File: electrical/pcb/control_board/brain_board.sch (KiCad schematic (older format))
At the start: 7 parts, among them J10 6posheader, J27 PPTC102LFBN-RC, J6 S9175-ND_rpi_breakout, J7 S9175-ND_rpi_breakout, J8 6posheader

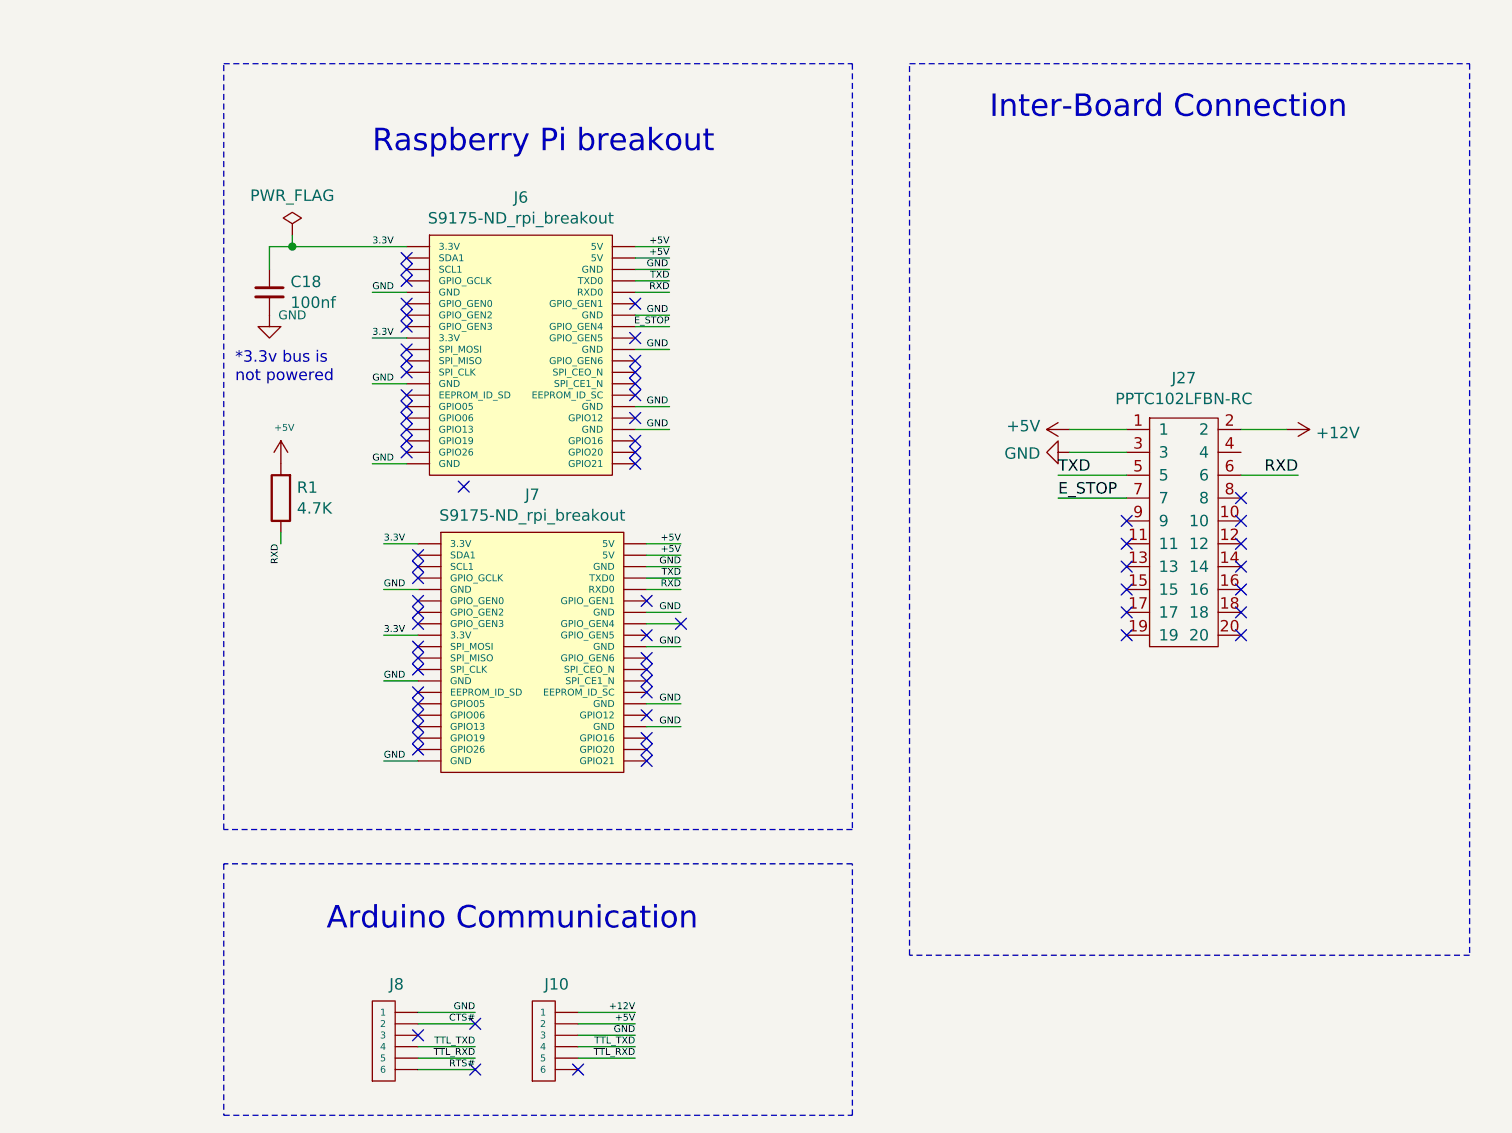
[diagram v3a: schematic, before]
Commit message: updating motor and brain boards with board-specific power nets
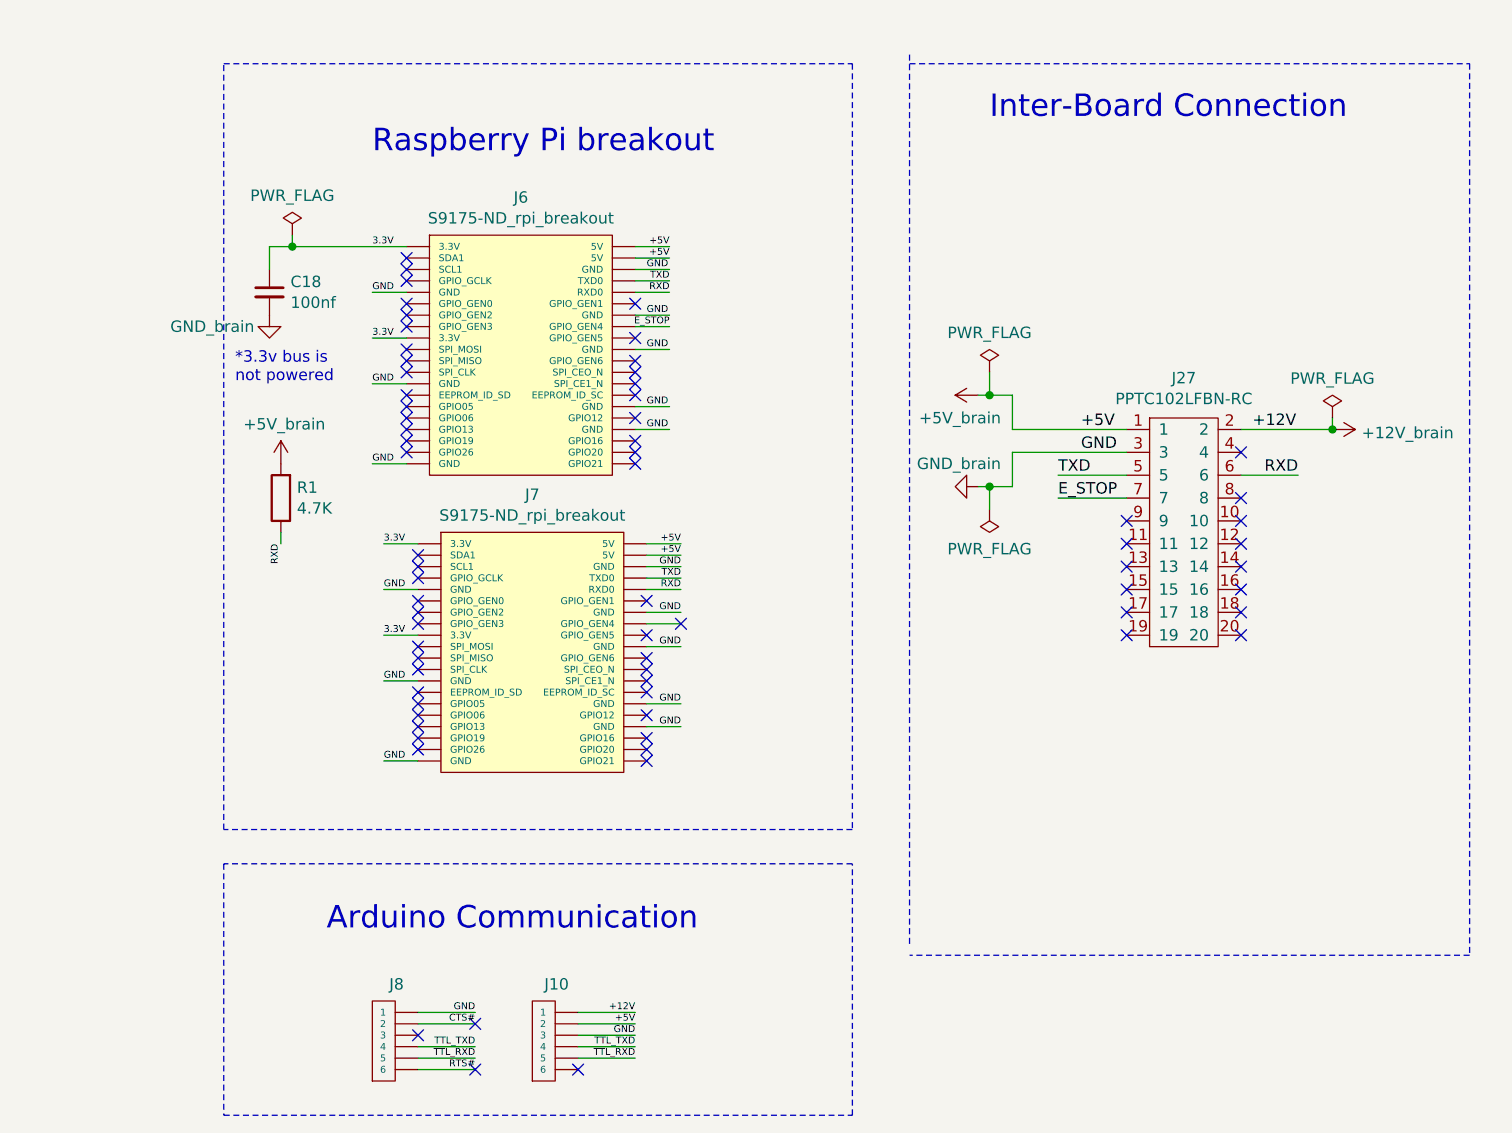
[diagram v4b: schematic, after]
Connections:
- net labels added: +12V_brain, +5V_brain, GND_brain
- wire segments 50 -> 59
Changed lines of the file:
@@
 Text Label 3250 3500 3    30   ~ 0
 RXD
-$Comp
-L power:+5V #PWR048
-U 1 1 60A8A8E0
-P 3250 3150
-F 0 "#PWR048" H 3250 3000 50  0001 C CNN
-F 1 "+5V" H 3265 3308 30  0000 C CNN
-F 2 "" H 3250 3150 50  0001 C CNN
-F 3 "" H 3250 3150 50  0001 C CNN
-	1    3250 3150
-	1    0    0    -1
-$EndComp
 Wire Wire Line
 	3250 3450 3250 3500
@@
 	1    0    0    -1
 $EndComp
-$Comp
-L power:GND #PWR047
-U 1 1 60A8A955
-P 3200 2500
-F 0 "#PWR047" H 3200 2250 50  0001 C CNN
-F 1 "GND" H 3300 2500 39  0000 C CNN
-F 2 "" H 3200 2500 50  0001 C CNN
-F 3 "" H 3200 2500 50  0001 C CNN
-	1    3200 2500
-	1    0    0    -1
-$EndComp
 Wire Wire Line
 	3200 2200 3300 2200
@@
 NoConn ~ 4100 5600
 NoConn ~ 5000 3850
-NoConn ~ 4050 3250
 NoConn ~ 3800 2650
 NoConn ~ 3800 2750
@@
 	8450 5300 6000 5300
 Wire Notes Line style solid rgb(0, 0, 0)
-	6000 5300 6000 1400
+	6000 5250 6000 1350
 Wire Notes Line style solid rgb(0, 0, 0)
 	6000 1400 8450 1400
 Text Notes 6350 1650 0    98   ~ 0
 Inter-Board Connection
-$Comp
-L power:+5V #PWR?
-U 1 1 60ED7C4A
-P 6700 3000
-AR Path="/60A51BAC/60ED7C4A" Ref="#PWR?"  Part="1"
-AR Path="/60A5279E/60ED7C4A" Ref="#PWR049"  Part="1"
-F 0 "#PWR049" H 6700 2850 50  0001 C CNN
-F 1 "+5V" V 6715 3128 50  0000 L CNN
-F 2 "" H 6700 3000 50  0001 C CNN
-F 3 "" H 6700 3000 50  0001 C CNN
-	1    6700 3000
-	0    -1   -1   0
-$EndComp
-$Comp
-L power:+12V #PWR?
-U 1 1 60ED7C50
-P 7650 3000
-AR Path="/60A51BAC/60ED7C50" Ref="#PWR?"  Part="1"
-AR Path="/60A5279E/60ED7C50" Ref="#PWR051"  Part="1"
-F 0 "#PWR051" H 7650 2850 50  0001 C CNN
-F 1 "+12V" V 7665 3128 50  0000 L CNN
-F 2 "" H 7650 3000 50  0001 C CNN
-F 3 "" H 7650 3000 50  0001 C CNN
-	1    7650 3000
-	0    1    1    0
-$EndComp
-$Comp
-L power:GND #PWR?
-U 1 1 60ED7C56
-P 6700 3100
-AR Path="/60A51BAC/60ED7C56" Ref="#PWR?"  Part="1"
-AR Path="/60A5279E/60ED7C56" Ref="#PWR050"  Part="1"
-F 0 "#PWR050" H 6700 2850 50  0001 C CNN
-F 1 "GND" V 6705 2972 50  0000 R CNN
-F 2 "" H 6700 3100 50  0001 C CNN
-F 3 "" H 6700 3100 50  0001 C CNN
-	1    6700 3100
-	0    1    1    0
-$EndComp
 Text Label 6650 3200 0    50   ~ 0
 TXD
@@
 E_STOP
 Wire Wire Line
-	6700 3000 6950 3000
-Wire Wire Line
-	6700 3100 6950 3100
-Wire Wire Line
 	6650 3200 6950 3200
 Wire Wire Line
@@
 Wire Wire Line
 	7450 3200 7700 3200
-Wire Wire Line
-	7450 3000 7650 3000
 $Comp
 L JPL_Robotics_Lib:PPTC102LFBN-RC J27
@@
 NoConn ~ 6950 3800
 NoConn ~ 6950 3900
+$Comp
+L JPL_Robotics_Lib:+5V_brain #PWR0144
+U 1 1 618E53AB
+P 3250 3150
+F 0 "#PWR0144" H 3250 3000 50  0001 C CNN
+F 1 "+5V_brain" H 3265 3323 50  0000 C CNN
+F 2 "" H 3250 3150 50  0001 C CNN
+F 3 "" H 3250 3150 50  0001 C CNN
+	1    3250 3150
+	1    0    0    -1
+$EndComp
+$Comp
+L JPL_Robotics_Lib:GND_brain #PWR0145
+U 1 1 618E86D3
+P 3200 2500
+F 0 "#PWR0145" H 3200 2250 50  0001 C CNN
+F 1 "GND_brain" H 2950 2450 50  0000 C CNN
+F 2 "" H 3200 2500 50  0001 C CNN
+F 3 "" H 3200 2500 50  0001 C CNN
+	1    3200 2500
+	1    0    0    -1
+$EndComp
+$Comp
+L JPL_Robotics_Lib:+5V_brain #PWR0146
+U 1 1 618ECDE5
+P 6300 2850
+F 0 "#PWR0146" H 6300 2700 50  0001 C CNN
+F 1 "+5V_brain" V 6200 2750 50  0000 L CNN
+F 2 "" H 6300 2850 50  0001 C CNN
+F 3 "" H 6300 2850 50  0001 C CNN
+	1    6300 2850
+	0    -1   -1   0
+$EndComp
+$Comp
+L JPL_Robotics_Lib:GND_brain #PWR0147
+U 1 1 618EE99B
+P 6300 3250
+F 0 "#PWR0147" H 6300 3000 50  0001 C CNN
+F 1 "GND_brain" V 6200 3350 50  0000 R CNN
+F 2 "" H 6300 3250 50  0001 C CNN
+F 3 "" H 6300 3250 50  0001 C CNN
+	1    6300 3250
+	0    1    1    0
+$EndComp
+$Comp
+L JPL_Robotics_Lib:+12V_brain #PWR0148
+U 1 1 618F0639
+P 7850 3000
+F 0 "#PWR0148" H 7850 2850 50  0001 C CNN
+F 1 "+12V_brain" V 7865 3128 50  0000 L CNN
+F 2 "" H 7850 3000 50  0001 C CNN
+F 3 "" H 7850 3000 50  0001 C CNN
+	1    7850 3000
+	0    1    1    0
+$EndComp
+Text Label 6750 3000 0    50   ~ 0
++5V
+Text Label 6750 3100 0    50   ~ 0
+GND
+Text Label 7500 3000 0    50   ~ 0
++12V
+NoConn ~ 7450 3100
+$Comp
+L power:PWR_FLAG #FLG0101
+U 1 1 6195B322
+P 6350 2750
+F 0 "#FLG0101" H 6350 2825 50  0001 C CNN
+F 1 "PWR_FLAG" H 6350 2923 50  0000 C CNN
+F 2 "" H 6350 2750 50  0001 C CNN
+F 3 "~" H 6350 2750 50  0001 C CNN
+	1    6350 2750
+	1    0    0    -1
+$EndComp
+$Comp
+L power:PWR_FLAG #FLG0102
+U 1 1 6195CC58
+P 6350 3350
+F 0 "#FLG0102" H 6350 3425 50  0001 C CNN
+F 1 "PWR_FLAG" H 6350 3523 50  0000 C CNN
+F 2 "" H 6350 3350 50  0001 C CNN
+F 3 "~" H 6350 3350 50  0001 C CNN
+	1    6350 3350
+	-1   0    0    1
+$EndComp
+Wire Wire Line
+	6450 3250 6350 3250
+Wire Wire Line
+	6450 3100 6950 3100
+Wire Wire Line
+	6350 3250 6350 3350
+Connection ~ 6350 3250
+Wire Wire Line
+	6350 3250 6300 3250
+Wire Wire Line
+	6450 2850 6350 2850
+Wire Wire Line
+	6450 3000 6950 3000
+Wire Wire Line
+	6350 2850 6350 2750
+Connection ~ 6350 2850
+Wire Wire Line
+	6350 2850 6300 2850
+Wire Wire Line
+	6450 3100 6450 3250
+Wire Wire Line
+	6450 2850 6450 3000
+Wire Wire Line
+	7450 3000 7850 3000
+$Comp
+L power:PWR_FLAG #FLG0103
+U 1 1 619765A5
+P 7850 2950
+F 0 "#FLG0103" H 7850 3025 50  0001 C CNN
+F 1 "PWR_FLAG" H 7850 3123 50  0000 C CNN
+F 2 "" H 7850 2950 50  0001 C CNN
+F 3 "~" H 7850 2950 50  0001 C CNN
+	1    7850 2950
+	1    0    0    -1
+$EndComp
+Wire Wire Line
+	7850 2950 7850 3000
+Connection ~ 7850 3000
 $EndSCHEMATC

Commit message: Adding footprints for male and female inter-board connectors
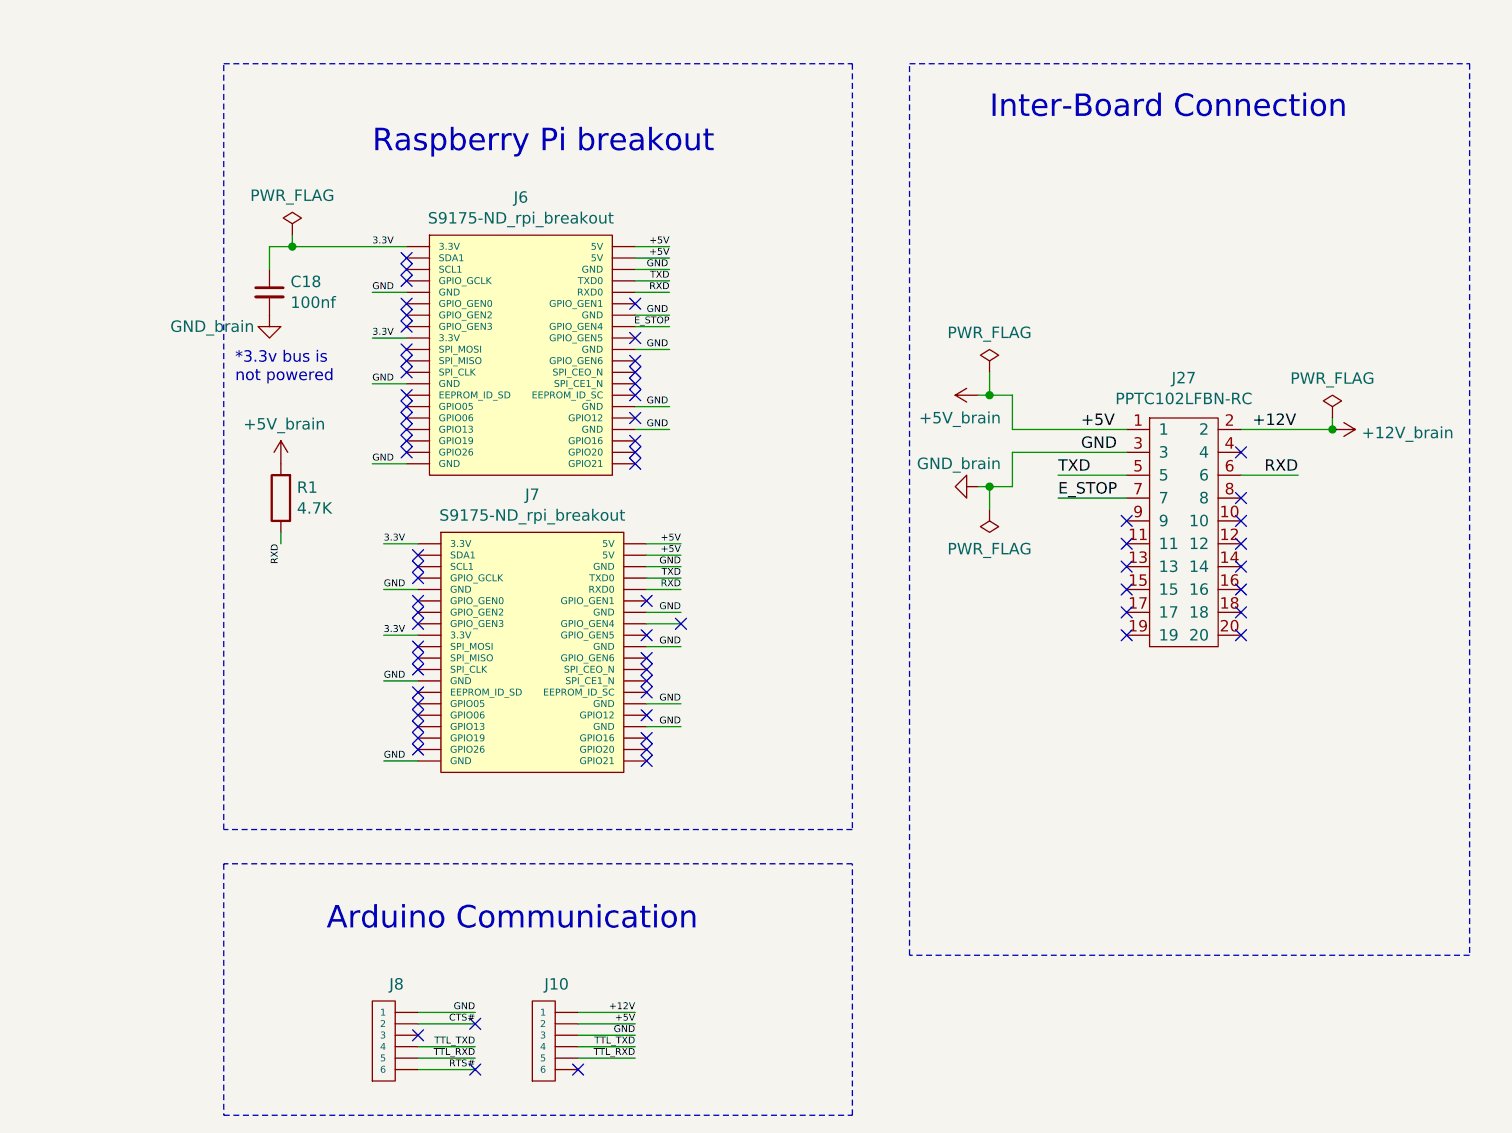
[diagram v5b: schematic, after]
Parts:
- J27: footprint (none) -> JPL Robotics:PPTC102LFBN-RC
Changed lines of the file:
@@
 	8450 5300 6000 5300
 Wire Notes Line style solid rgb(0, 0, 0)
-	6000 5250 6000 1350
+	6000 5300 6000 1400
 Wire Notes Line style solid rgb(0, 0, 0)
 	6000 1400 8450 1400
@@
 F 0 "J27" H 7200 2925 50  0000 C CNN
 F 1 "PPTC102LFBN-RC" H 7200 2834 50  0000 C CNN
-F 2 "" H 7500 2850 50  0001 C CNN
+F 2 "JPL Robotics:PPTC102LFBN-RC" H 7500 2850 50  0001 C CNN
 F 3 "" H 7500 2850 50  0001 C CNN
 	1    7200 2850
